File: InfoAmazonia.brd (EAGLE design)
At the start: 95.2 x 74.3 mm, 80 parts, among them IC1 LM2662, IC2 ADAFRUIT FONA, IC3 MIC29302AWD, IC4 4050D, IC5 TL032C, IC6 CA3140AM Z, IC7 TL081BCDG4, IC8 SHT20, IC9 NE555, J1 BNCPTH, J2 BNCPTH, J3 BNCPTH, U1 ARDUINO-MEGAPRO, U2 MPL3115A2, U3 USD-SOCKETNEW, U4 ALS-PT19

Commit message: - Mudanças bem minimas (Valores de capacitor por exemplo)
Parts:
- C4, C5: value 220uF -> 47uF
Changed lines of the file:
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@@
 <?xml version="1.0" encoding="utf-8"?>
 <!DOCTYPE eagle SYSTEM "eagle.dtd">
-<eagle version="7.3.0">
+<eagle version="7.2.0">
 <drawing>
 <settings>
@@
 <attribute name="VALUE" x="9.525" y="8.89" size="1.27" layer="27" font="vector" ratio="15"/>
 </element>
-<element name="C5" library="InfoAmazonia" package="UD-6,3X5,8_NICHICON" value="220uF" x="4.445" y="14.605" smashed="yes">
+<element name="C5" library="InfoAmazonia" package="UD-6,3X5,8_NICHICON" value="47uF" x="4.445" y="14.605" smashed="yes">
 <attribute name="NAME" x="1.27" y="18.415" size="1.016" layer="25" font="vector" ratio="15"/>
 <attribute name="VALUE" x="1.27" y="10.16" size="1.016" layer="27" font="vector" ratio="15"/>
 </element>
-<element name="C4" library="InfoAmazonia" package="UD-6,3X5,8_NICHICON" value="220uF" x="4.445" y="22.225" smashed="yes">
+<element name="C4" library="InfoAmazonia" package="UD-6,3X5,8_NICHICON" value="47uF" x="4.445" y="22.225" smashed="yes">
 <attribute name="NAME" x="1.27" y="26.035" size="1.016" layer="25" font="vector" ratio="15"/>
 <attribute name="VALUE" x="1.27" y="17.78" size="1.016" layer="27" font="vector" ratio="15"/>
@@
 <wire x1="71.4375" y1="8.73125" x2="70.485" y2="7.77875" width="0.4064" layer="1"/>
 <wire x1="70.485" y1="7.77875" x2="70.485" y2="7.2" width="0.4064" layer="1"/>
-<wire x1="25.4" y1="2.54" x2="25.4" y2="2.38125" width="0.4064" layer="16"/>
-<wire x1="25.4" y1="2.38125" x2="26.9875" y2="0.79375" width="0.4064" layer="16"/>
-<wire x1="26.9875" y1="0.79375" x2="49.53" y2="0.79375" width="0.4064" layer="16"/>
 <via x="49.53" y="0.79375" extent="1-16" drill="0.5"/>
+<wire x1="25.4" y1="0.79375" x2="49.53" y2="0.79375" width="0.4064" layer="16"/>
 <wire x1="49.53" y1="0.79375" x2="59.69" y2="0.79375" width="0.4064" layer="1"/>
 <wire x1="59.69" y1="0.79375" x2="60.80125" y2="1.905" width="0.4064" layer="1"/>
 <wire x1="60.80125" y1="1.905" x2="60.80125" y2="5.98875" width="0.4064" layer="1"/>
 <wire x1="60.80125" y1="5.98875" x2="59.69" y2="7.1" width="0.4064" layer="1"/>
-<wire x1="25.4" y1="2.54" x2="25.4" y2="1.5875" width="0.4064" layer="16"/>
-<wire x1="25.4" y1="1.5875" x2="24.28875" y2="0.79375" width="0.4064" layer="16"/>
-<wire x1="24.28875" y1="0.79375" x2="9.942534375" y2="0.79375" width="0.4064" layer="16"/>
+<wire x1="25.4" y1="0.79375" x2="9.942534375" y2="0.79375" width="0.4064" layer="16"/>
 <wire x1="9.942534375" y1="0.79375" x2="8.255" y2="2.481284375" width="0.4064" layer="16"/>
 <wire x1="8.255" y1="2.481284375" x2="8.255" y2="8.89" width="0.4064" layer="16"/>
@@
 <wire x1="7.46125" y1="9.68375" x2="7.46125" y2="38.4175" width="0.4064" layer="16"/>
 <wire x1="7.46125" y1="38.4175" x2="7.62" y2="38.57625" width="0.4064" layer="16"/>
+<wire x1="25.4" y1="2.54" x2="25.4" y2="0.79375" width="0.4064" layer="16"/>
 </signal>
 <signal name="N$2">

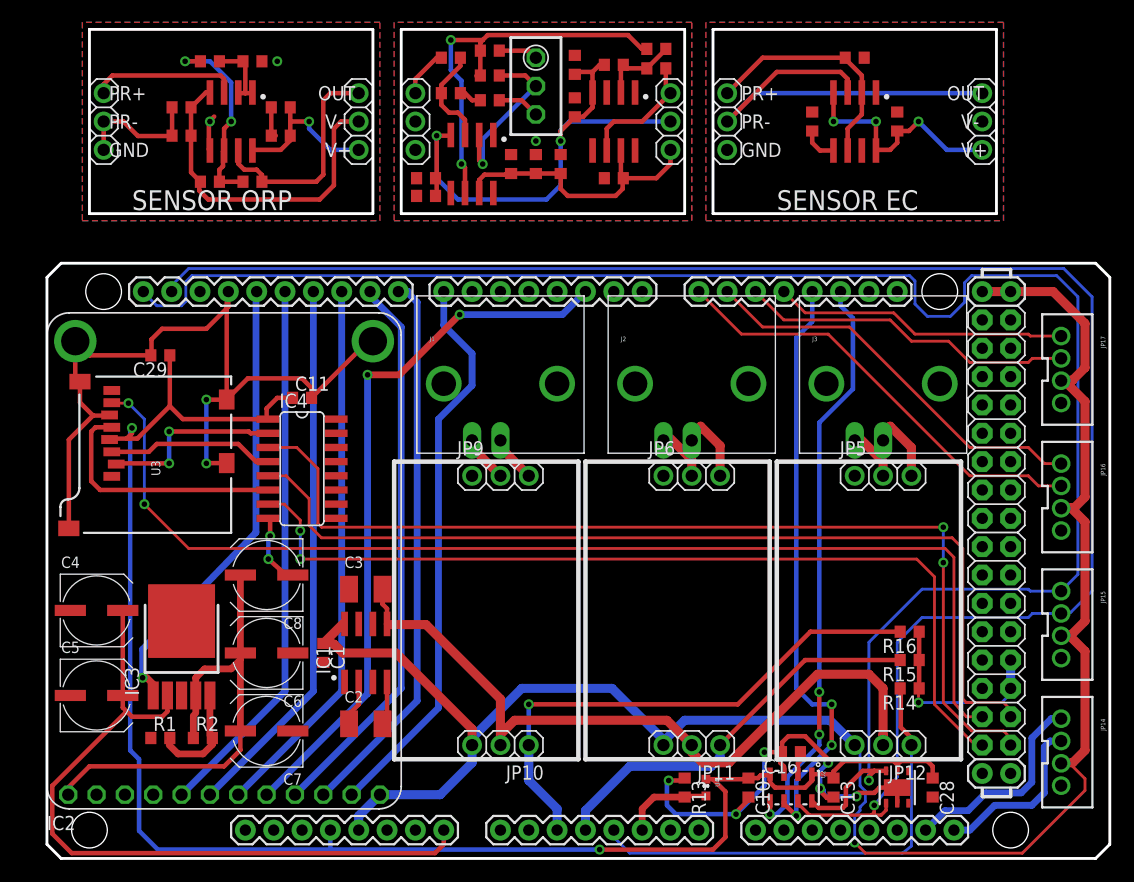
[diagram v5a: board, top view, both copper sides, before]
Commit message: - Agora os modulos tem tamanho definido via componente nas bibliotecas
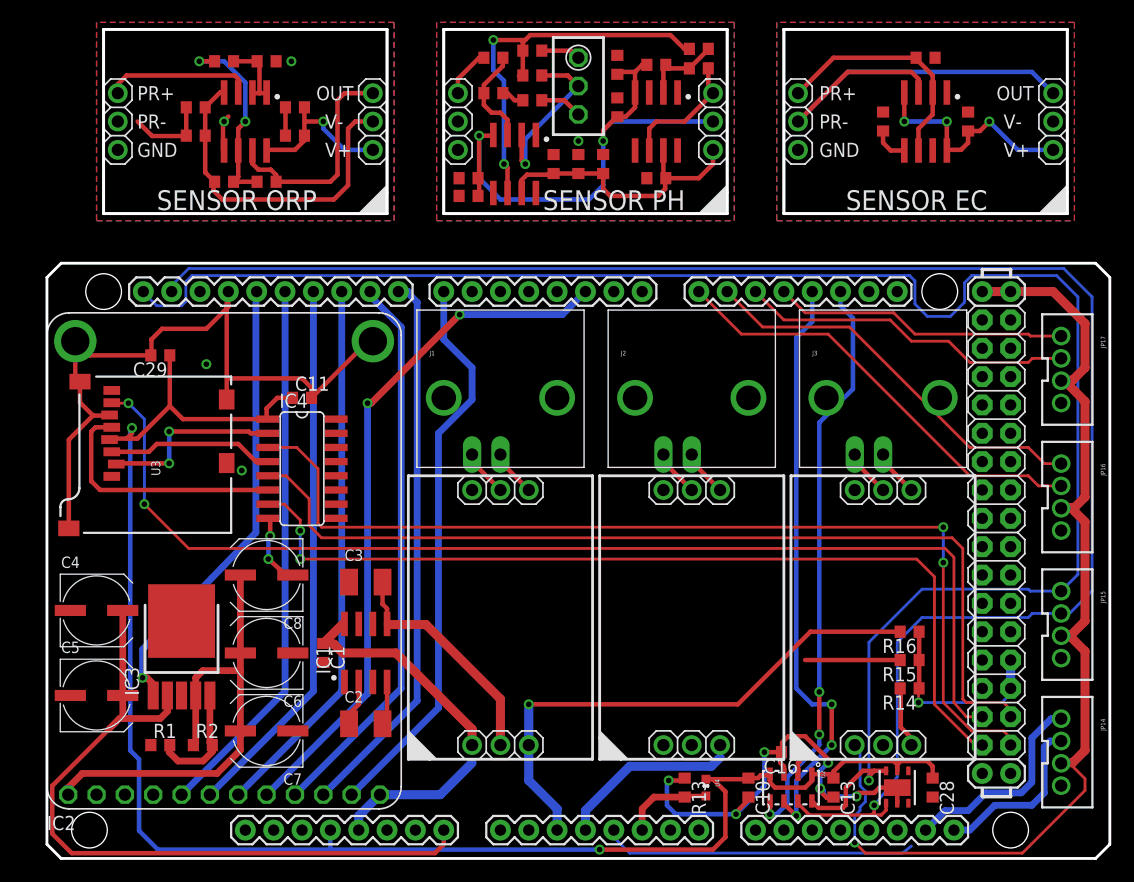
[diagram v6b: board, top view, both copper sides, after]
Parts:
- removed JP1, JP10, JP11, JP12, JP2, JP3, JP4, JP5, JP6, JP7, JP8, JP9: (no value), InfoAmazonia:1X03
- added MD1, MD2, MD3, MD6: INFO-AMAZONIA-MODULE, InfoAmazonia:INFO-AMAZONIA-MODULE
- added MD4, MD5: (no value), InfoAmazonia:INFO-AMAZONIA-MODULE
- moved C30 6.35 mm to (74.9, 66.0)
- moved C31 6.35 mm to (82.5, 66.0)
- moved C32 6.35 mm to (78.7, 71.8)
- moved IC9 6.35 mm to (78.7, 66.0)
- moved C12 3.81 mm to (47.6, 62.2)
- moved C15 3.81 mm to (37.8, 61.0)
- moved C18 3.81 mm to (37.8, 59.4)
- moved C19 3.81 mm to (40.0, 68.6)
- moved C20 3.81 mm to (43.5, 70.2)
- moved C22 3.81 mm to (54.6, 61.0)
- moved C24 3.81 mm to (51.1, 67.3)
- moved C26 3.81 mm to (51.1, 71.1)
- moved C9 3.81 mm to (45.4, 62.2)
- moved IC7 3.81 mm to (54.6, 66.0)
- moved R10 3.81 mm to (54.6, 71.1)
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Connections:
- net +5V: now also MD1.1, MD2.1, MD3.1; no longer JP10.3, JP11.3, JP12.3
- net +VEC: now also MD6.1; no longer JP3.3
- net +VORP: now also MD5.1; no longer JP7.3
- net +VPH: now also MD4.1; no longer JP1.3
- net -5V: now also MD1.2, MD2.2, MD3.2, MD6.2; no longer JP10.2, JP11.2, JP12.2
- net -VORP: now also MD5.2; no longer JP7.2
- net -VPH: now also MD4.2; no longer JP1.2
- net 1_SENSOR: now also MD1.3; no longer JP10.1
- net 2_SENSOR: now also MD2.3; no longer JP11.1
- net 3_SENSOR: now also MD3.3; no longer JP12.1
- net EC_IN: now also MD6.4; no longer JP4.3
- net EC_SENSOR: now also MD6.3, MD6.5; no longer JP3.1, JP4.2
- net GND: now also MD1.6, MD2.6, MD3.6, MD4.5, MD4.6, MD5.5, MD5.6, MD6.6; no longer JP2.1, JP2.2, JP4.1, JP5.1, JP6.1, JP8.1, JP8.2, JP9.1
- net N$1: now also J1.GND, MD1.5; no longer J1.S, JP9.3
- net N$11: now also J2.GND, MD2.5; no longer J2.S, JP6.3
- net N$12: now also J2.S, MD2.4; no longer J2.GND, JP6.2
- net N$13: now also J3.GND, MD3.5; no longer J3.S, JP5.3
- net N$22: now also J3.S, MD3.4; no longer J3.GND, JP5.2
- net N$9: now also J1.S, MD1.4; no longer J1.GND, JP9.2
- net ORP_IN: now also MD5.4; no longer JP8.3
- net ORP_SENSOR: now also MD5.3; no longer JP7.1
- net PH_IN: now also MD4.4; no longer JP2.3
- net PH_SENSOR: now also MD4.3; no longer JP1.1
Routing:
- net -5V: track 67.9 -> 21.0 mm
- net +5V: track 172.8 -> 129.4 mm
- net GND: track 143.5 -> 128.7 mm
- net 2_SENSOR: track 36.2 -> 24.3 mm
- net 3_SENSOR: track 42.8 -> 33.1 mm
- net N$11: track 6.67 -> 4.23 mm
- net N$13: track 6.65 -> 4.23 mm
- net N$12: track 5.81 -> 4.23 mm
- net EC_SENSOR: track 38.0 -> 39.6 mm
- net GSM_RI: track 64.0 -> 62.5 mm
- net N$22: track 5.50 -> 4.23 mm
- net N$18: track 9.70 -> 10.3 mm
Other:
- outline, holes or cut-outs redrawn
- board text added: "SENSOR PH"

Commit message: - Mudanca no pino rx/tx do fona
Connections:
- removed net GSM_RX: IC2.10, U1.8
- removed net GSM_TX: IC2.9, U1.9
- net RX2: now also IC2.9; no longer JP17.1
- net TX2: now also IC2.10; no longer JP17.2
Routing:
- net GSM_TX: track 50.2 -> 0.00 mm
- net GSM_RX: track 49.9 -> 0.00 mm
- net 2_SENSOR: track 24.3 -> 36.2 mm
- net 3_SENSOR: track 33.1 -> 42.9 mm
- net +5V: track 129.4 -> 132.8 mm
- net RX2: track 26.5 -> 23.7 mm
- net TX2: track 30.2 -> 27.6 mm
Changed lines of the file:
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@@
 <wire x1="90.89" y1="8.525" x2="91.64625" y2="8.525" width="0.254" layer="1"/>
 <wire x1="91.64625" y1="8.525" x2="93.0275" y2="7.14375" width="0.254" layer="1"/>
-<wire x1="93.0275" y1="7.14375" x2="93.0275" y2="6.093396875" width="0.254" layer="1"/>
-<wire x1="93.0275" y1="6.093396875" x2="87.410353125" y2="0.47625" width="0.254" layer="1"/>
-<wire x1="87.410353125" y1="0.47625" x2="73.3425" y2="0.47625" width="0.254" layer="1"/>
+<wire x1="93.0275" y1="7.14375" x2="93.0275" y2="4.188396875" width="0.254" layer="1"/>
+<wire x1="93.0275" y1="4.188396875" x2="89.315353125" y2="0.47625" width="0.254" layer="1"/>
+<wire x1="89.315353125" y1="0.47625" x2="73.3425" y2="0.47625" width="0.254" layer="1"/>
 <wire x1="73.3425" y1="0.47625" x2="72.39" y2="1.42875" width="0.254" layer="1"/>
 <via x="72.39" y="1.42875" extent="1-16" drill="0.5"/>
@@
 <contactref element="MD2" pad="1"/>
 <contactref element="MD3" pad="1"/>
-<wire x1="72.86625" y1="9.68375" x2="72.39" y2="10.16" width="0" layer="19" extent="16-16"/>
+<wire x1="38.1" y1="8.5725" x2="38.1" y2="10.16" width="0.8128" layer="16"/>
+<wire x1="72.86625" y1="9.68375" x2="72.39" y2="10.16" width="0.4064" layer="16"/>
 <wire x1="55.245" y1="10.16" x2="72.39" y2="10.16" width="0" layer="19" extent="1-1"/>
 <wire x1="38.1" y1="10.16" x2="55.245" y2="10.16" width="0" layer="19" extent="1-1"/>
-<wire x1="38.1" y1="8.5725" x2="38.1" y2="10.16" width="0" layer="19" extent="16-16"/>
 </signal>
 <signal name="+3V3">
@@
 <wire x1="35.56" y1="46.51375" x2="35.56" y2="50.8" width="0.6096" layer="16"/>
 </signal>
-<signal name="GSM_RX">
-<contactref element="IC2" pad="10"/>
-<contactref element="U1" pad="8"/>
-<wire x1="24.765" y1="5.715" x2="33.17875" y2="14.12875" width="0.6096" layer="16"/>
-<wire x1="33.17875" y1="14.12875" x2="33.17875" y2="49.8475" width="0.6096" layer="16"/>
-<wire x1="31.59125" y1="50.8" x2="31.496" y2="50.8" width="0.6096" layer="16"/>
-<wire x1="33.17875" y1="49.8475" x2="32.385" y2="50.64125" width="0.6096" layer="16"/>
-<wire x1="32.385" y1="50.64125" x2="32.385" y2="50.8" width="0.6096" layer="16"/>
-<wire x1="31.496" y1="50.8" x2="32.385" y2="50.8" width="0.6096" layer="16"/>
-</signal>
-<signal name="GSM_TX">
-<contactref element="IC2" pad="9"/>
-<contactref element="U1" pad="9"/>
-<wire x1="22.225" y1="5.715" x2="31.75" y2="15.24" width="0.6096" layer="16"/>
-<wire x1="31.75" y1="15.24" x2="31.75" y2="47.625" width="0.6096" layer="16"/>
-<wire x1="31.75" y1="47.625" x2="28.956" y2="50.419" width="0.6096" layer="16"/>
-<wire x1="28.956" y1="50.419" x2="28.956" y2="50.8" width="0.6096" layer="16"/>
-</signal>
 <signal name="GSM_RI">
 <contactref element="IC2" pad="8"/>
@@
 <wire x1="76.46125" y1="17.78" x2="67.945" y2="17.78" width="0.4064" layer="1"/>
 <contactref element="MD2" pad="3"/>
-<wire x1="60.325" y1="10.16" x2="67.945" y2="17.78" width="0" layer="19" extent="1-1"/>
-<wire x1="60.325" y1="9.04875" x2="60.325" y2="10.16" width="0" layer="19" extent="16-16"/>
+<wire x1="67.945" y1="17.78" x2="60.325" y2="10.16" width="0.4064" layer="1"/>
+<wire x1="60.325" y1="9.04875" x2="60.325" y2="10.16" width="0.8128" layer="16"/>
 </signal>
 <signal name="3_SENSOR">
 <contactref element="U1" pad="A4"/>
 <contactref element="R14" pad="2"/>
-<wire x1="76.67625" y1="0.47625" x2="52.22875" y2="0.47625" width="0.254" layer="16"/>
-<wire x1="77.47" y1="1.11125" x2="76.67625" y2="0.47625" width="0.254" layer="16"/>
+<wire x1="76.835" y1="0.47625" x2="52.22875" y2="0.47625" width="0.254" layer="16"/>
+<wire x1="77.47" y1="1.11125" x2="76.835" y2="0.47625" width="0.254" layer="16"/>
 <wire x1="76.35875" y1="15.1375" x2="76.46125" y2="15.24" width="0.4064" layer="1"/>
 <wire x1="77.47" y1="10.795" x2="76.5175" y2="11.7475" width="0.4064" layer="1"/>
@@
 <wire x1="50.8" y1="1.905" x2="50.8" y2="2.54" width="0.254" layer="16"/>
 <contactref element="MD3" pad="3"/>
-<wire x1="77.47" y1="10.16" x2="77.47" y2="10.795" width="0" layer="19" extent="1-1"/>
-<wire x1="77.47" y1="1.11125" x2="77.47" y2="10.16" width="0" layer="19" extent="16-16"/>
+<wire x1="77.47" y1="10.795" x2="77.47" y2="10.16" width="0.4064" layer="1"/>
+<wire x1="77.47" y1="1.11125" x2="77.47" y2="10.16" width="0.254" layer="16"/>
 </signal>
 <signal name="TEMP_SENSOR">
@@
 <wire x1="90.89" y1="33.385" x2="88.8525" y2="33.385" width="0.254" layer="1"/>
 <wire x1="88.8525" y1="33.385" x2="87.9475" y2="34.29" width="0.254" layer="1"/>
-<wire x1="87.9475" y1="34.29" x2="82.70875" y2="34.29" width="0.254" layer="1"/>
-<wire x1="82.70875" y1="34.29" x2="70.00875" y2="46.99" width="0.254" layer="1"/>
-<wire x1="70.00875" y1="46.99" x2="62.23" y2="46.99" width="0.254" layer="1"/>
+<wire x1="87.9475" y1="34.29" x2="81.43875" y2="34.29" width="0.254" layer="1"/>
+<wire x1="81.43875" y1="34.29" x2="68.73875" y2="46.99" width="0.254" layer="1"/>
+<wire x1="68.73875" y1="46.99" x2="62.23" y2="46.99" width="0.254" layer="1"/>
 <wire x1="62.23" y1="46.99" x2="58.42" y2="50.8" width="0.254" layer="1"/>
 </signal>
@@
 <wire x1="90.89" y1="35.385" x2="89.3925" y2="35.385" width="0.254" layer="1"/>
 <wire x1="89.3925" y1="35.385" x2="87.9475" y2="36.83" width="0.254" layer="1"/>
-<wire x1="87.9475" y1="36.83" x2="82.70875" y2="36.83" width="0.254" layer="1"/>
-<wire x1="82.70875" y1="36.83" x2="71.91375" y2="47.625" width="0.254" layer="1"/>
-<wire x1="71.91375" y1="47.625" x2="64.135" y2="47.625" width="0.254" layer="1"/>
+<wire x1="87.9475" y1="36.83" x2="80.80375" y2="36.83" width="0.254" layer="1"/>
+<wire x1="80.80375" y1="36.83" x2="70.00875" y2="47.625" width="0.254" layer="1"/>
+<wire x1="70.00875" y1="47.625" x2="64.135" y2="47.625" width="0.254" layer="1"/>
 <wire x1="64.135" y1="47.625" x2="60.96" y2="50.8" width="0.254" layer="1"/>
 </signal>
 <signal name="TX2">
 <contactref element="U1" pad="16"/>
-<contactref element="JP17" pad="2"/>
-<wire x1="90.89" y1="44.815" x2="88.3125" y2="44.815" width="0.254" layer="1"/>
 <wire x1="88.3125" y1="44.815" x2="87.9475" y2="44.45" width="0.254" layer="1"/>
-<wire x1="87.9475" y1="44.45" x2="82.70875" y2="44.45" width="0.254" layer="1"/>
-<wire x1="82.70875" y1="44.45" x2="80.80375" y2="46.355" width="0.254" layer="1"/>
-<wire x1="80.80375" y1="46.355" x2="77.47" y2="46.355" width="0.254" layer="1"/>
-<wire x1="77.47" y1="46.355" x2="75.565" y2="48.26" width="0.254" layer="1"/>
-<wire x1="75.565" y1="48.26" x2="66.04" y2="48.26" width="0.254" layer="1"/>
+<wire x1="87.9475" y1="44.45" x2="74.93" y2="44.45" width="0.254" layer="1"/>
+<wire x1="74.93" y1="44.45" x2="71.12" y2="48.26" width="0.254" layer="1"/>
+<wire x1="71.12" y1="48.26" x2="66.04" y2="48.26" width="0.254" layer="1"/>
 <wire x1="66.04" y1="48.26" x2="63.5" y2="50.8" width="0.254" layer="1"/>
+<contactref element="IC2" pad="10"/>
+<wire x1="24.765" y1="5.715" x2="66.04" y2="48.26" width="0" layer="19" extent="1-1"/>
 </signal>
 <signal name="RX2">
 <contactref element="U1" pad="17"/>
-<contactref element="JP17" pad="1"/>
-<wire x1="90.89" y1="46.815" x2="88.1225" y2="46.815" width="0.254" layer="1"/>
 <wire x1="88.1225" y1="46.815" x2="87.9475" y2="46.99" width="0.254" layer="1"/>
-<wire x1="87.9475" y1="46.99" x2="77.7875" y2="46.99" width="0.254" layer="1"/>
-<wire x1="77.7875" y1="46.99" x2="75.8825" y2="48.895" width="0.254" layer="1"/>
-<wire x1="75.8825" y1="48.895" x2="67.945" y2="48.895" width="0.254" layer="1"/>
+<wire x1="87.9475" y1="46.99" x2="73.9775" y2="46.99" width="0.254" layer="1"/>
+<wire x1="73.9775" y1="46.99" x2="72.0725" y2="48.895" width="0.254" layer="1"/>
+<wire x1="72.0725" y1="48.895" x2="67.945" y2="48.895" width="0.254" layer="1"/>
 <wire x1="67.945" y1="48.895" x2="66.04" y2="50.8" width="0.254" layer="1"/>
+<contactref element="IC2" pad="9"/>
+<wire x1="22.225" y1="5.715" x2="66.04" y2="50.8" width="0" layer="19" extent="1-1"/>
 </signal>
 <signal name="+12V">

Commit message: -
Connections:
- removed net TEMP_SENSOR: U1.A6
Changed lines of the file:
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@@
 <wire x1="77.47" y1="1.11125" x2="77.47" y2="10.16" width="0.254" layer="16"/>
-</signal>
-<signal name="TEMP_SENSOR">
-<contactref element="U1" pad="A6"/>
 </signal>
 <signal name="A15">
